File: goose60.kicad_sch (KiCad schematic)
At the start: 23 parts, among them SW1 SW_Push, SW2 SW_Push, U1 STM32F103CBTx, X1 Crystal_GND24

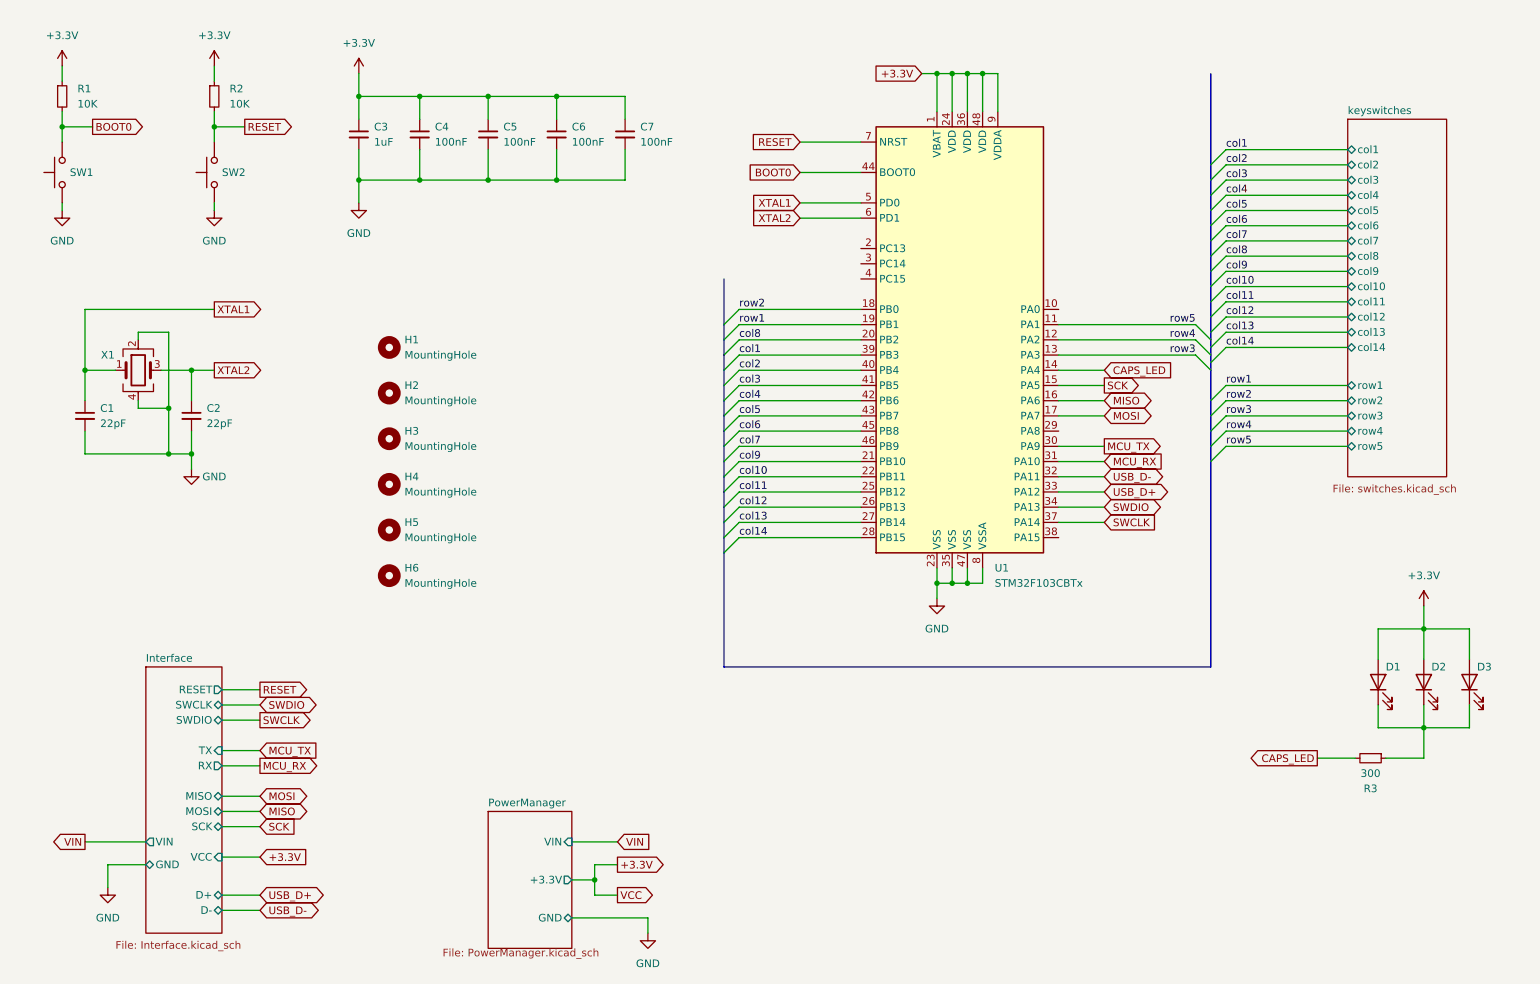
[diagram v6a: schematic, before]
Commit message: add res and fix rule check fail problom
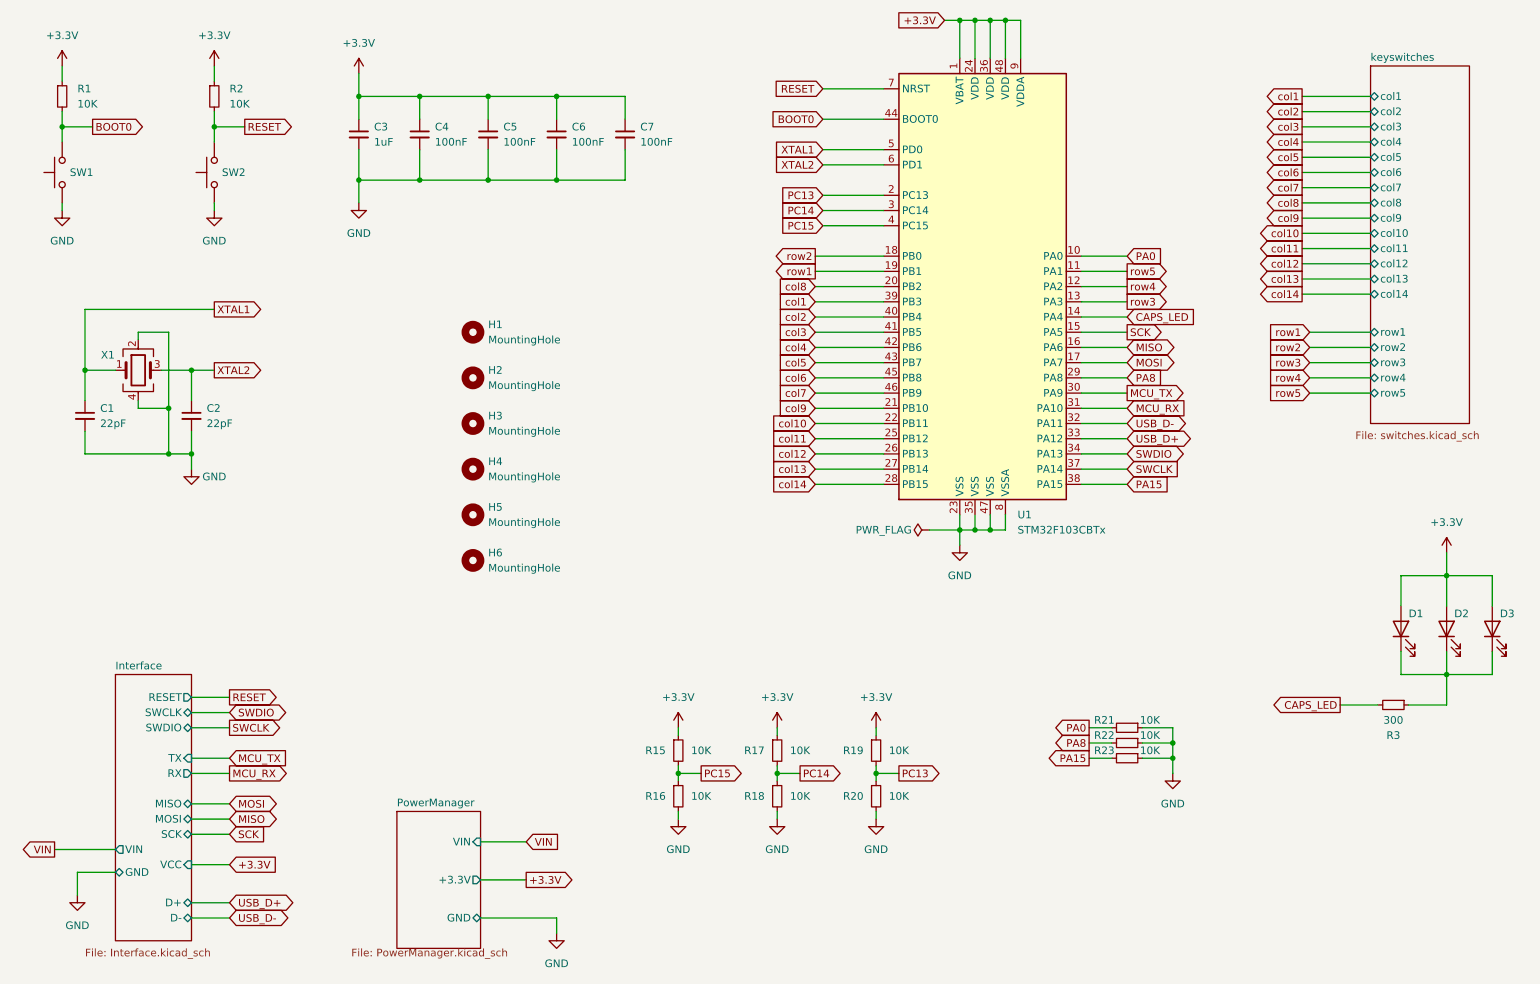
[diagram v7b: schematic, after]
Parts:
- added R15, R16, R17, R18, R19, R20, R21, R22, R23: 10K, Resistor_SMD:R_0603_1608Metric, symbol Device:R_Small
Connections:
- net +3.3V: now also R15.1, R17.1, R19.1
- net GND: now also R16.2, R18.2, R20.2, R21.1, R22.1, R23.1
- net PA0: now reaches U1.10 (PA0)
- net PA0: now also R21.2
- net PC13: now reaches U1.2 (PC13)
- net PC13: now also R19.2, R20.1
- net PA8: now reaches U1.29 (PA8)
- net PA8: now also R22.2
- net PC14: now reaches U1.3 (PC14)
- net PC14: now also R17.2, R18.1
- net PA15: now reaches U1.38 (PA15)
- net PA15: now also R23.2
- net PC15: now reaches U1.4 (PC15)
- net PC15: now also R15.2, R16.1
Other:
- moved on the sheet: D1, D2, D3, H1, H2, H3, H4, H5, H6, R3, U1

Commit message: change pin default and try layout
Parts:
- H2, H3, H5, H6: footprint MountingHole:MountingHole_3.2mm_M3_Pad -> MountingHole:MountingHole_3.2mm_M3_Pad_TopOnly
- H4: footprint MountingHole:MountingHole_3.2mm_M3 -> MountingHole:MountingHole_3.2mm_M3_Pad_TopOnly
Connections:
- net CAPS_LED: now also U1.29 (PA8); no longer U1.14 (PA4)
- net col1: now also U1.27 (PB14); no longer U1.39 (PB3)
- net col10: now also U1.46 (PB9); no longer U1.22 (PB11)
- net col11: now also U1.22 (PB11); no longer U1.25 (PB12)
- net col12: now also U1.21 (PB10); no longer U1.26 (PB13)
- net col13: now also U1.20 (PB2); no longer U1.27 (PB14)
- net col14: now also U1.18 (PB0); no longer U1.28 (PB15)
- net col2: now also U1.26 (PB13); no longer U1.40 (PB4)
- net col3: now also U1.25 (PB12); no longer U1.41 (PB5)
- net col4: now also U1.28 (PB15); no longer U1.42 (PB6)
- net col5: now also U1.39 (PB3); no longer U1.43 (PB7)
- net col6: now also U1.40 (PB4); no longer U1.45 (PB8)
- net col7: now also U1.41 (PB5); no longer U1.46 (PB9)
- net col8: now also U1.42 (PB6); no longer U1.20 (PB2)
- net col9: now also U1.43 (PB7); no longer U1.21 (PB10)
- net row2: now also U1.45 (PB8); no longer U1.18 (PB0)
- net PA8 renamed PA4
- net PA4: now also U1.14 (PA4); no longer U1.29 (PA8)
